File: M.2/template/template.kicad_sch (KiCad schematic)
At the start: 3 parts

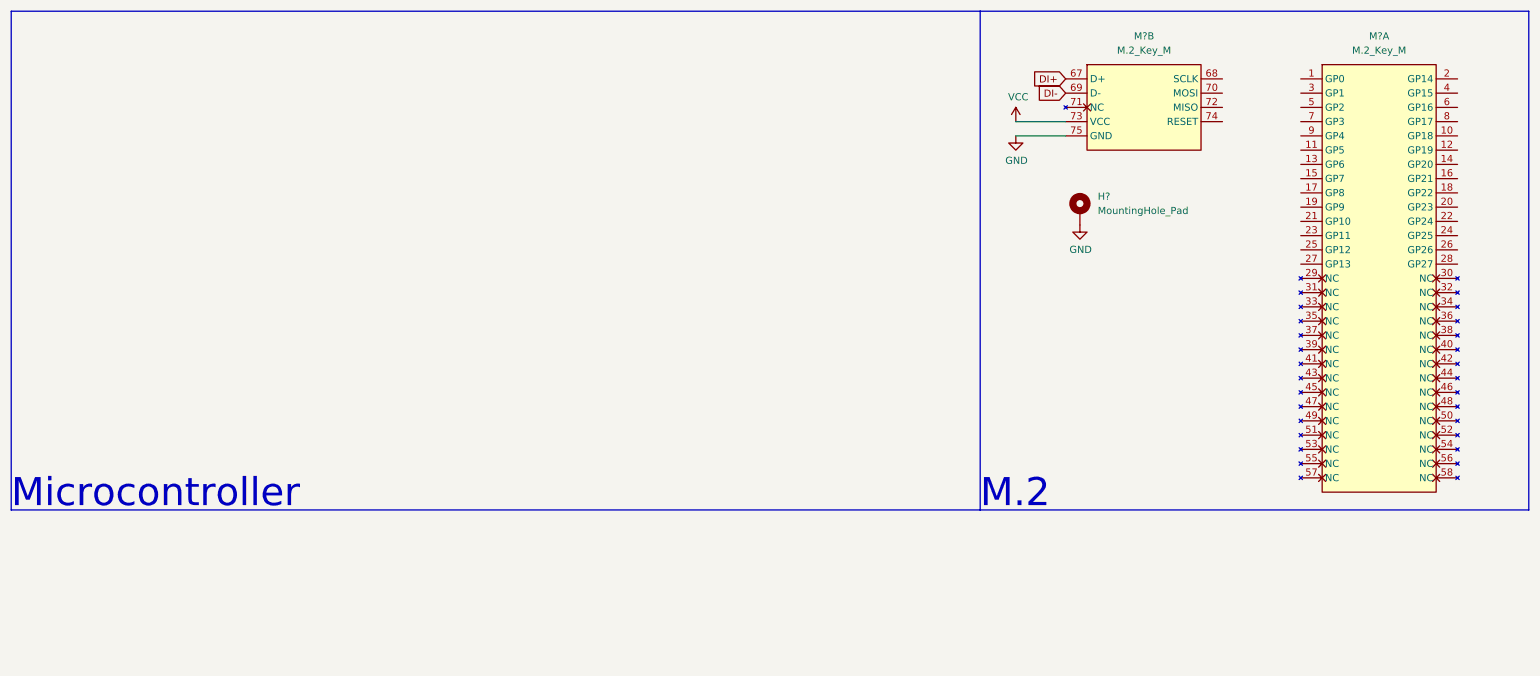
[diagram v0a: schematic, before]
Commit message: change the rest to key e, change the template
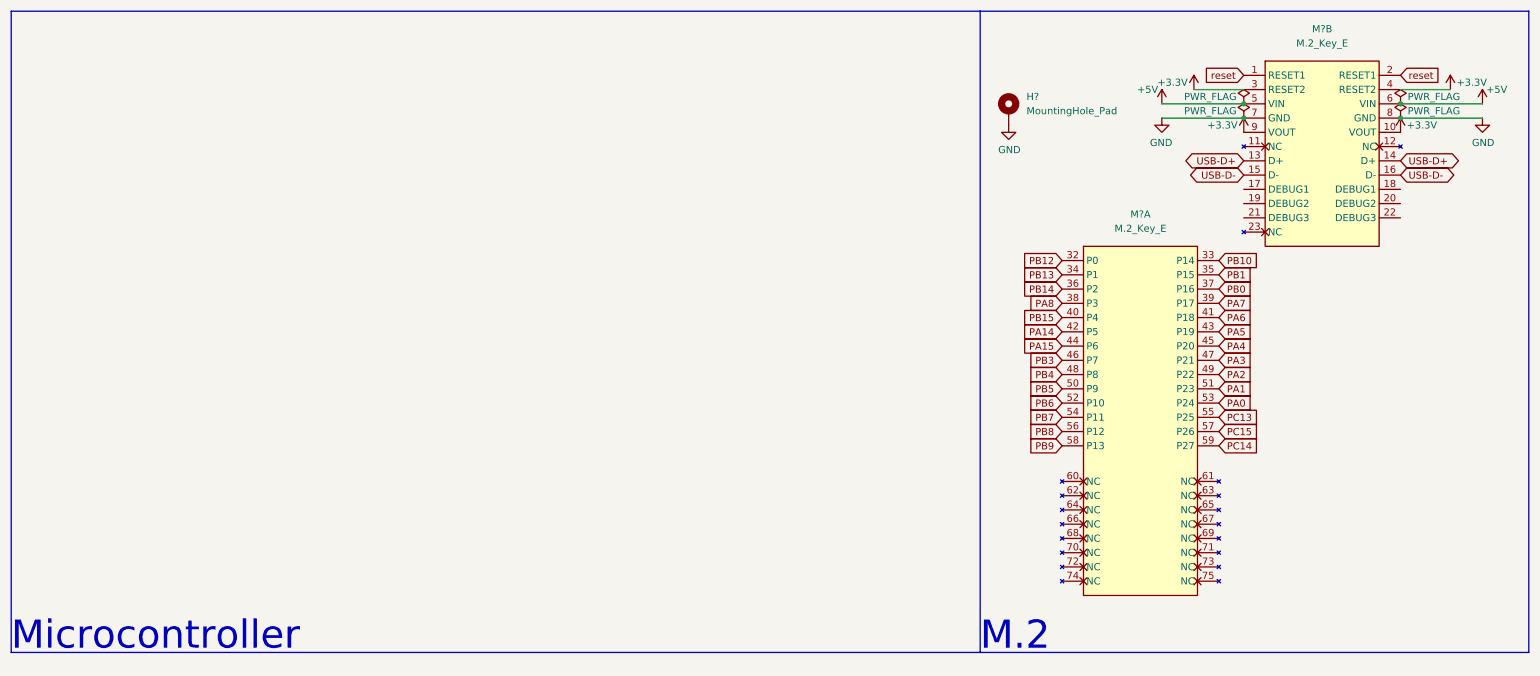
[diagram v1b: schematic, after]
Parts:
- removed H?: MountingHole_Pad, MountingHole:MountingHole_2.2mm_M2_ISO7380_Pad, symbol Mechanical:MountingHole_Pad
- removed M? (x2): M.2_Key_M, m2ngff:m2-padKeyM, symbol m2ngff:M.2_Key_M
- added H?: MountingHole_Pad, MountingHole:MountingHole_2.2mm_M2_ISO7380_Pad, symbol Mechanical:MountingHole_Pad
- added M? (x2): M.2_Key_E, m2ngff:m2-padKeyE, symbol m2ngff:M.2_Key_E
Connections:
- net GND: now also H?.1, M?.7 (GND), M?.8 (GND)
- new net +3V3: M?.10 (VOUT), M?.3 (RESET2), M?.4 (RESET2), M?.9 (VOUT)
- new net +5V: M?.5 (VIN), M?.6 (VIN)
- new net PA0: M?.53 (P24)
- new net PA1: M?.51 (P23)
- new net PA14: M?.42 (P5)
- new net PA15: M?.44 (P6)
- new net PA2: M?.49 (P22)
- new net PA3: M?.47 (P21)
- new net PA4: M?.45 (P20)
- new net PA5: M?.43 (P19)
- new net PA6: M?.41 (P18)
- new net PA7: M?.39 (P17)
- new net PA8: M?.38 (P3)
- new net PB0: M?.37 (P16)
- new net PB1: M?.35 (P15)
- new net PB10: M?.33 (P14)
- new net PB12: M?.32 (P0)
- new net PB13: M?.34 (P1)
- new net PB14: M?.36 (P2)
- new net PB15: M?.40 (P4)
- new net PB3: M?.46 (P7)
- new net PB4: M?.48 (P8)
- new net PB5: M?.50 (P9)
- new net PB6: M?.52 (P10)
- new net PB7: M?.54 (P11)
- new net PB8: M?.56 (P12)
- new net PB9: M?.58 (P13)
- new net PC13: M?.55 (P25)
- new net PC14: M?.59 (P27)
- new net PC15: M?.57 (P26)
- new net USB-D+: M?.13 (D+), M?.14 (D+)
- new net USB-D-: M?.15 (D-), M?.16 (D-)
- new net reset: M?.1 (RESET1), M?.2 (RESET1)

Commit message: finish working on stmf411
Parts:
- removed H?: MountingHole_Pad, MountingHole:MountingHole_2.2mm_M2_ISO7380_Pad, symbol Mechanical:MountingHole_Pad
- added H?: MountingHole_Pad, MountingHole:MountingHole_2.2mm_M2_Pad_Via, symbol Mechanical:MountingHole_Pad
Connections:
- net GND: now also H?.1
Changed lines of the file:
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@@
+    (pin "1")
+  )
+  (symbol (lib_id "Power:GND") (at 191.135 29.21 0) (unit 1)
+    (in_bom yes) (on_board yes)
+    (property "Reference" "#PWR?" (id 0) (at 191.135 35.56 0)
+      (effects (font (size 1.27 1.27)) hide)
+    )
+    (property "Value" "GND" (id 1) (at 191.262 33.6042 0))
+    (property "Footprint" "" (id 2) (at 191.135 29.21 0)
+      (effects (font (size 1.27 1.27)) hide)
+    )
+    (property "Datasheet" "" (id 3) (at 191.135 29.21 0)
+      (effects (font (size 1.27 1.27)) hide)
+    )
     (pin "1")
   )
@@
     (pin "1")
   )
-  (symbol (lib_id "Power:GND") (at 191.135 33.655 0) (unit 1)
-    (in_bom yes) (on_board yes)
-    (property "Reference" "#PWR?" (id 0) (at 191.135 40.005 0)
-      (effects (font (size 1.27 1.27)) hide)
-    )
-    (property "Value" "GND" (id 1) (at 191.262 38.0492 0))
-    (property "Footprint" "" (id 2) (at 191.135 33.655 0)
-      (effects (font (size 1.27 1.27)) hide)
-    )
-    (property "Datasheet" "" (id 3) (at 191.135 33.655 0)
-      (effects (font (size 1.27 1.27)) hide)
-    )
-    (pin "1")
-  )
-  (symbol (lib_id "Mechanical:MountingHole_Pad") (at 191.135 31.115 0) (unit 1)
-    (in_bom yes) (on_board yes) (fields_autoplaced)
-    (property "Reference" "H?" (id 0) (at 194.31 28.5749 0)
-      (effects (font (size 1.27 1.27)) (justify left))
-    )
-    (property "Value" "MountingHole_Pad" (id 1) (at 194.31 31.1149 0)
-      (effects (font (size 1.27 1.27)) (justify left))
-    )
-    (property "Footprint" "MountingHole:MountingHole_2.2mm_M2_ISO7380_Pad" (id 2) (at 191.135 31.115 0)
-      (effects (font (size 1.27 1.27)) hide)
-    )
-    (property "Datasheet" "~" (id 3) (at 191.135 31.115 0)
-      (effects (font (size 1.27 1.27)) hide)
-    )
-    (pin "1")
-  )
   (symbol (lib_id "power:+3.3V") (at 233.045 34.925 0) (mirror y) (unit 1)
     (in_bom yes) (on_board yes)
@@
     )
     (property "Datasheet" "" (id 3) (at 224.155 27.305 0)
+      (effects (font (size 1.27 1.27)) hide)
+    )
+    (pin "1")
+  )
+  (symbol (lib_id "Mechanical:MountingHole_Pad") (at 191.135 26.67 0) (unit 1)
+    (in_bom yes) (on_board yes) (fields_autoplaced)
+    (property "Reference" "H?" (id 0) (at 194.31 24.1299 0)
+      (effects (font (size 1.27 1.27)) (justify left))
+    )
+    (property "Value" "MountingHole_Pad" (id 1) (at 194.31 26.6699 0)
+      (effects (font (size 1.27 1.27)) (justify left))
+    )
+    (property "Footprint" "MountingHole:MountingHole_2.2mm_M2_Pad_Via" (id 2) (at 191.135 26.67 0)
+      (effects (font (size 1.27 1.27)) hide)
+    )
+    (property "Datasheet" "~" (id 3) (at 191.135 26.67 0)
       (effects (font (size 1.27 1.27)) hide)
     )
@@
       (reference "#PWR?") (unit 1) (value "+3.3V") (footprint "")
     )
+    (path "/71079b24-2e2e-494b-a607-86ccdae75c6e"
+      (reference "#PWR?") (unit 1) (value "GND") (footprint "")
+    )
     (path "/7b58219a-a31d-4ba4-804a-77c6d706d8bc"
       (reference "#PWR?") (unit 1) (value "GND") (footprint "")
@@
       (reference "#PWR?") (unit 1) (value "+5V") (footprint "")
     )
-    (path "/94a21413-9821-4587-923e-f37548a5150a"
-      (reference "#PWR?") (unit 1) (value "GND") (footprint "")
-    )
     (path "/9d4bb085-5413-4cad-9765-4f916ffbe612"
       (reference "#PWR?") (unit 1) (value "+3.3V") (footprint "")
@@
       (reference "#PWR?") (unit 1) (value "+3.3V") (footprint "")
     )
-    (path "/9c7af13e-949e-4a55-a6b7-45ef51b4f106"
-      (reference "H?") (unit 1) (value "MountingHole_Pad") (footprint "MountingHole:MountingHole_2.2mm_M2_ISO7380_Pad")
+    (path "/f46fb303-7470-41c0-b6e8-4553c1d6503f"
+      (reference "H?") (unit 1) (value "MountingHole_Pad") (footprint "MountingHole:MountingHole_2.2mm_M2_Pad_Via")
     )
     (path "/2792ed93-89db-4e51-99ff-281323e776eb"
